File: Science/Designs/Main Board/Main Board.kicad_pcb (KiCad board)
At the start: 2 copper layers, 127 x 101.6 mm, 93 parts, among them J1 I2C_OUT, J10 AIR_SENS, J11 MOISTURE_SENS, J12 LIMIT3, J13 LIMIT2, J14 LIMIT1, J15 SERVO3, J16 SERVO2, J17 SERVO1, J18 MOTOR1_SIG, J19 MOTOR2_SIG, J2 ANE_SENS, J20 MOTOR3_SIG, J4 ENCODER2, J5 ENCODER1, J7 ATMO_SENS, P1 LS7366R, P2 LS7366R, P3 RPI_HEADER, P4 PWR_IN, P5 UV_SENS, P6 DIST_SENS, P7 I2C_TEST, P8 THERMO_SENS, P9 SPI_TEST, U1 SN74HC14N, U2 TLV2544ID, U3 PCA9685, U4 PCA9685, U5 ACPL-064L-500E, U6 ACPL-064L-500E, U7 LM317T, Y1 20MHz, Y2 20MHz

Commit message: Layout nearing completion.
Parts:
- C1, C16, C17, C2, C3, C8, R1, R13, R2, R3, R37, R38, R39, R4, R5, R6, U1, U5, U6: moved to B.Cu
- moved R6 80.1 mm to (131.4, 59.1), turned to 270 degrees
- moved C3 78.1 mm to (127.6, 59.1), turned to 90 degrees
- moved R5 75.4 mm to (122.6, 59.1), turned to 270 degrees
- moved C8 75.1 mm to (116.2, 73.0), turned to 180 degrees
- moved C2 74.1 mm to (118.7, 59.1), turned to 90 degrees
- moved U1 73.7 mm to (116.2, 67.3)
- moved R4 72.3 mm to (113.7, 59.1), turned to 270 degrees
- moved C1 71.9 mm to (109.9, 59.1), turned to 90 degrees
- moved C17 53.3 mm to (111.8, 122.6), turned to 180 degrees
- moved C16 51.9 mm to (111.8, 132.7), turned to 180 degrees
- moved R1 49.5 mm to (140.3, 106.7), turned to 180 degrees
- moved R3 47.5 mm to (132.7, 106.7), turned to 0 degrees
- moved R2 46.7 mm to (140.3, 92.7), turned to 180 degrees
- moved U6 45.7 mm to (111.8, 117.5), turned to 0 degrees
- moved R13 44.6 mm to (132.7, 92.7), turned to 0 degrees
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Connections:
- P3 pad 16: /PI_SS_0 -> /PI_SS_3
- P3 pad 18: /PI_SS_1 -> /PI_SS_2
- P3 pad 29: /PI_SS_2 -> /PI_SS_1
- P3 pad 31: /PI_SS_3 -> /PI_SS_0
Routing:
- net +3V3: track 176.4 -> 320.4 mm
- net /ENC1_A: track 0.00 -> 111.3 mm, vias 0 -> 1
- net /PI_SCL: track 66.4 -> 172.0 mm, vias 2 -> 3
- net /PI_SDA: track 70.8 -> 172.0 mm, vias 2 -> 3
- net /MOTOR3_OUT: track 0.00 -> 100.2 mm
- net /ENC1_B: track 0.00 -> 90.5 mm, vias 0 -> 1
- net /MOTOR2_OUT: track 0.00 -> 89.2 mm
- net /MOTOR1_OUT: track 0.00 -> 79.0 mm
- net /PI_SS_0: track 0.00 -> 74.2 mm, vias 0 -> 2
- net /LIM3_OUT: track 0.00 -> 70.5 mm, vias 0 -> 1
- net /LIM2_OUT: track 0.00 -> 65.1 mm, vias 0 -> 1
- net /LIM1_OUT: track 0.00 -> 61.6 mm, vias 0 -> 1
- net /PI_SS_1: track 0.00 -> 53.0 mm
- net /PI_SCK: track 98.3 -> 142.8 mm
- net /PI_MISO: track 100.8 -> 142.7 mm
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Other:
- board text added: "AIRQ"
- board text added: "ANEM"
- board text added: "ATMO"
- board text added: "DIST"
- board text added: "ENC1"
- board text added: "ENC2"
- board text added: "I2C"
- board text added: "LIM1"
- board text added: "LIM2"
- board text added: "LIM3"
- board text added: "MOIST"
- board text added: "MOT1"
- board text added: "MOT2"
- board text added: "MOT3"
- board text added: "SERV1"
- board text added: "SERV2"
- board text added: "SERV3"
- board text added: "THERM"
- board text added: "UV"
- board text removed: "1"
- board text removed: "2"
- board text removed: "3"
- board text removed: "ENCODER"
- board text removed: "LIMIT SW"

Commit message: Continued work on main board layout. Nearing completion!
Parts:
- C18, C19, R40, R41: moved to B.Cu
- moved U7 51.2 mm to (124.5, 111.1), turned to 90 degrees
- moved C18 15.3 mm to (169.9, 87.9), turned to 90 degrees
- moved R40 8.62 mm to (172.4, 101.9), turned to 0 degrees
- moved HS1 7.16 mm to (121.0, 108.6)
- moved C19 6.74 mm to (177.5, 94.3), turned to 270 degrees
- moved R41 5.22 mm to (172.4, 98.7), turned to 0 degrees
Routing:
- net +5V: track 46.2 -> 213.3 mm
- net /PI_MISO: track 142.7 -> 257.7 mm, vias 0 -> 2
- net /PI_SCK: track 142.8 -> 239.5 mm, vias 0 -> 1
- net /PI_MOSI: track 66.6 -> 155.1 mm, vias 1 -> 3
- net +12V: track 0.00 -> 79.1 mm
- net +3V3: track 320.4 -> 395.9 mm, vias 0 -> 4
- net /PI_SDA: track 172.0 -> 183.1 mm
- net /PI_SCL: track 172.0 -> 182.5 mm
- net /LIM2_RAW: track 26.7 -> 22.5 mm
- net /ENC1_A: track 111.3 -> 110.6 mm
- net /LED_6R: track 19.7 -> 19.0 mm
- net /LED_3R: track 26.9 -> 27.6 mm
- net /RGB_5R: track 27.2 -> 26.4 mm

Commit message: Continuing layout work
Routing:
- net /ENC2_A: track 0.00 -> 104.0 mm, vias 0 -> 1
- net /ENC2_B: track 0.00 -> 98.3 mm, vias 0 -> 1
- net +3V3: track 395.9 -> 462.6 mm, vias 4 -> 6
- net +5V: track 213.3 -> 242.6 mm, vias 0 -> 1
- net /ENC1_B: track 90.5 -> 103.9 mm
- net /PI_SDA: track 183.1 -> 189.0 mm, vias 3 -> 5
- net /PI_SCL: track 182.5 -> 188.0 mm, vias 3 -> 5
- net /ENC1_A: track 110.6 -> 107.0 mm
- net /PI_MISO: track 257.7 -> 254.9 mm
- net /PI_MOSI: track 155.1 -> 152.6 mm
- net /PI_SCK: track 239.5 -> 237.0 mm

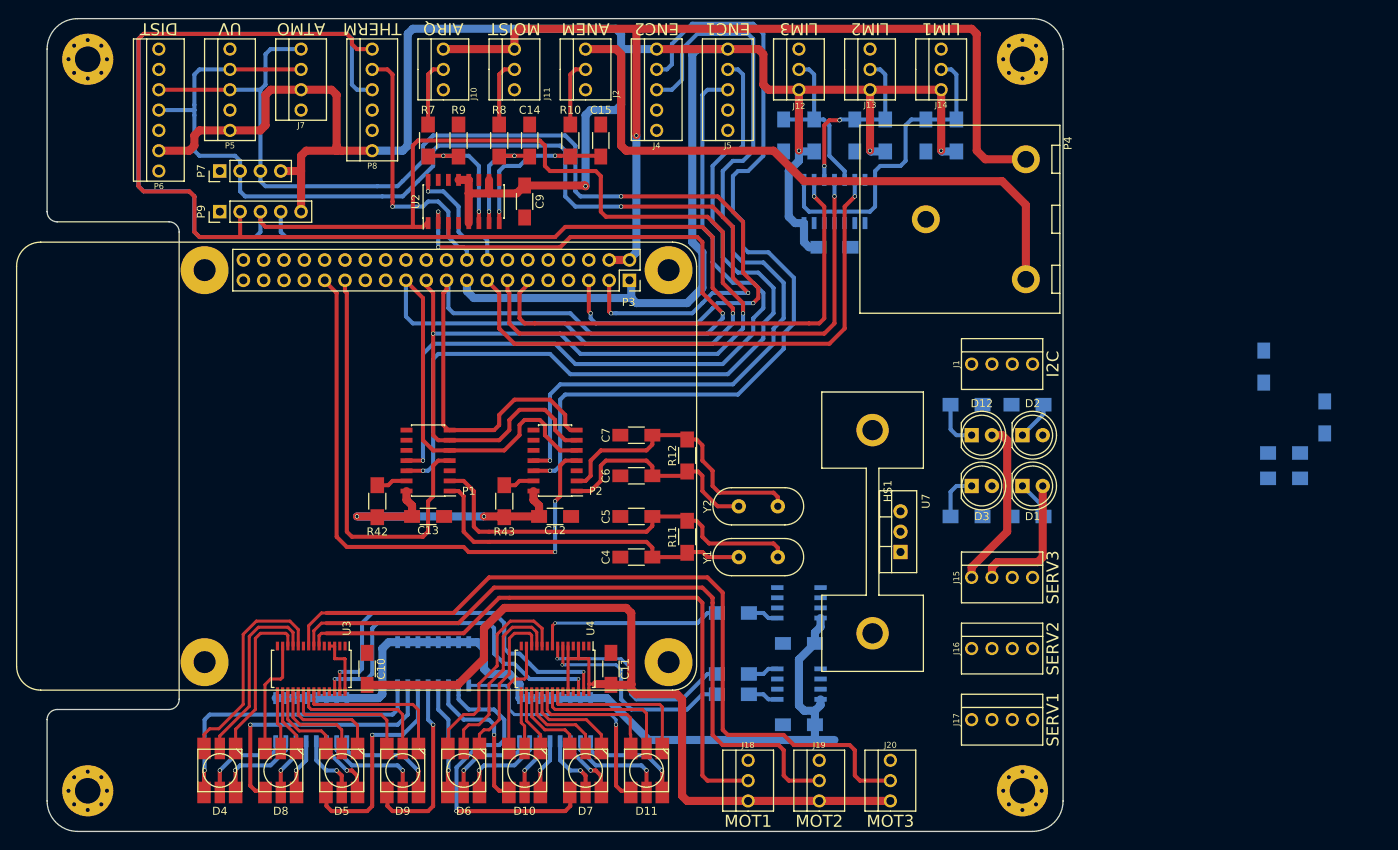
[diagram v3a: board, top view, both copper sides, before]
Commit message: Very close to finished main board
Just needs ground plane work now!
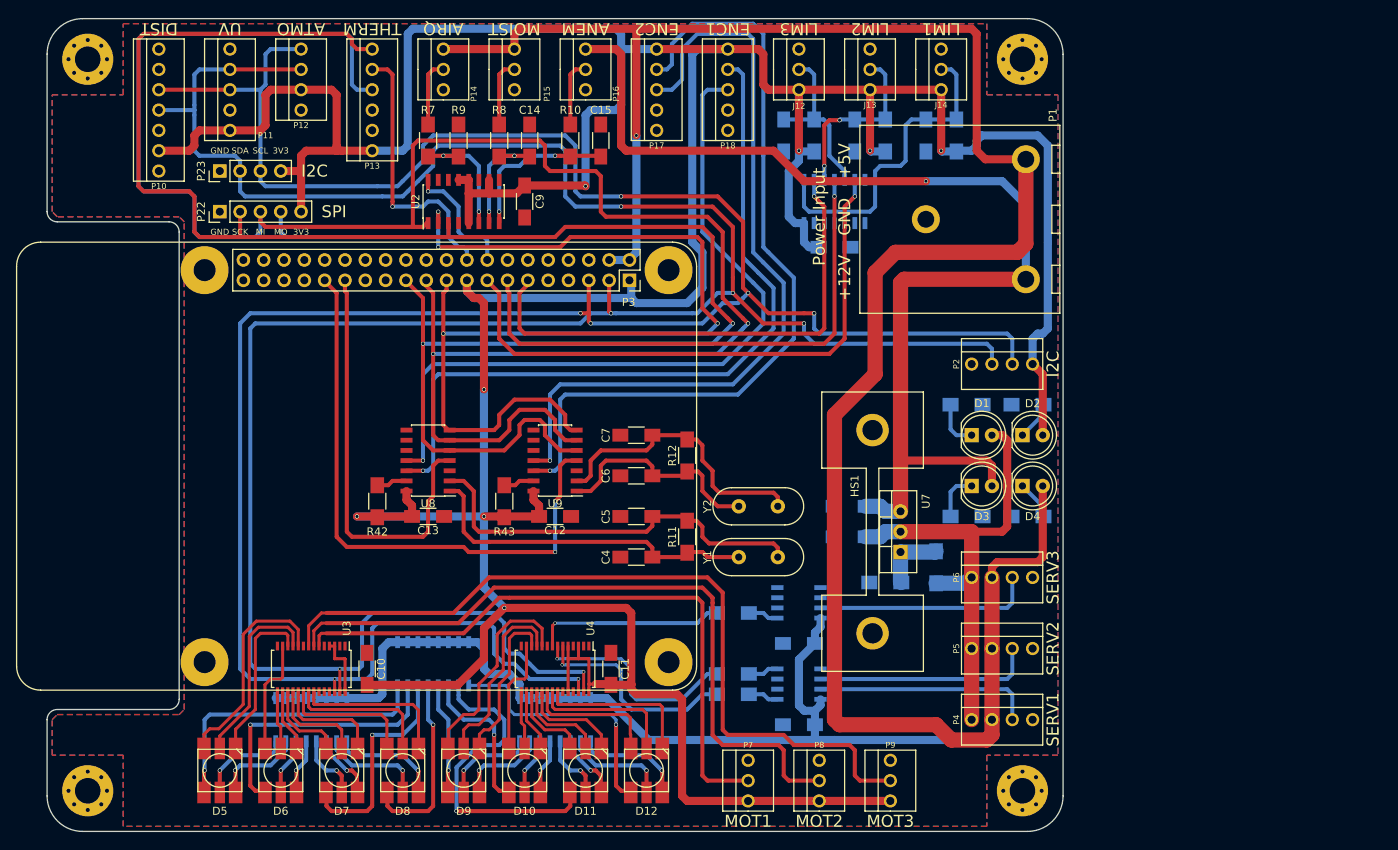
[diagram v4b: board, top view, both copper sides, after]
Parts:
- removed the P1 at (65.4, 99.7)
- removed the P2 at (81.3, 99.7)
- added U8: LS7366R, Housings_SOIC:SOIC-14_3.9x8.7mm_Pitch1.27mm, F.Cu at (65.4, 99.7)
- added U9: LS7366R, Housings_SOIC:SOIC-14_3.9x8.7mm_Pitch1.27mm, F.Cu at (81.3, 99.7)
- moved C19 61.2 mm to (118.1, 109.2), turned to 180 degrees
- moved C18 54.6 mm to (118.1, 105.4), turned to 180 degrees
- moved R40 51.5 mm to (122.6, 114.9)
- moved R41 45.8 mm to (128.9, 113.0), turned to 90 degrees
- renumbered D12 to D1, D7 to D11, D11 to D12, D1 to D4, D4 to D5, D8 to D6, D5 to D7, D9 to D8, D6 to D9, P4 to P1, P6 to P10, P5 to P11, J7 to P12, P8 to P13, J10 to P14, J11 to P15, J2 to P16, J4 to P17, J5 to P18, J1 to P2, P9 to P22, P7 to P23, J17 to P4, J16 to P5, J15 to P6, J18 to P7, J19 to P8, J20 to P9
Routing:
- net +5V: track 242.6 -> 394.0 mm
- net /PI_SCL: track 188.0 -> 325.5 mm, vias 5 -> 7
- net /PI_SDA: track 189.0 -> 323.4 mm, vias 5 -> 6
- net +3V3: track 462.6 -> 556.9 mm, vias 6 -> 8
- net +12V: track 79.1 -> 142.4 mm, vias 0 -> 1
- net /7.2V: track 21.2 -> 59.4 mm
- net /SERVO1_PWM: track 0.00 -> 27.4 mm
- net /SERVO3_PWM: track 0.00 -> 27.4 mm
- net /SERVO2_PWM: track 0.00 -> 27.4 mm
- net /ENC2_A: track 104.0 -> 95.1 mm
- net Net-(R40-Pad2): track 0.00 -> 8.33 mm
- net /PI_SCK: track 237.0 -> 228.9 mm, vias 1 -> 2
- net /ENC1_B: track 103.9 -> 98.5 mm
- net /ENC1_A: track 107.0 -> 101.6 mm
- net /ENC2_B: track 98.3 -> 93.2 mm
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- added copper zone on B.Cu, net GNDD
- added copper zone on F.Cu, net GNDD
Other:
- outline, holes or cut-outs redrawn
- board text added: "+12V"
- board text added: "+5V"
- board text added: "3V3"
- board text added: "GND"
- board text added: "MI"
- board text added: "MO"
- board text added: "Power Input"
- board text added: "SCK"
- board text added: "SCL"
- board text added: "SDA"
- board text added: "SPI"

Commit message: Ground planes almost done
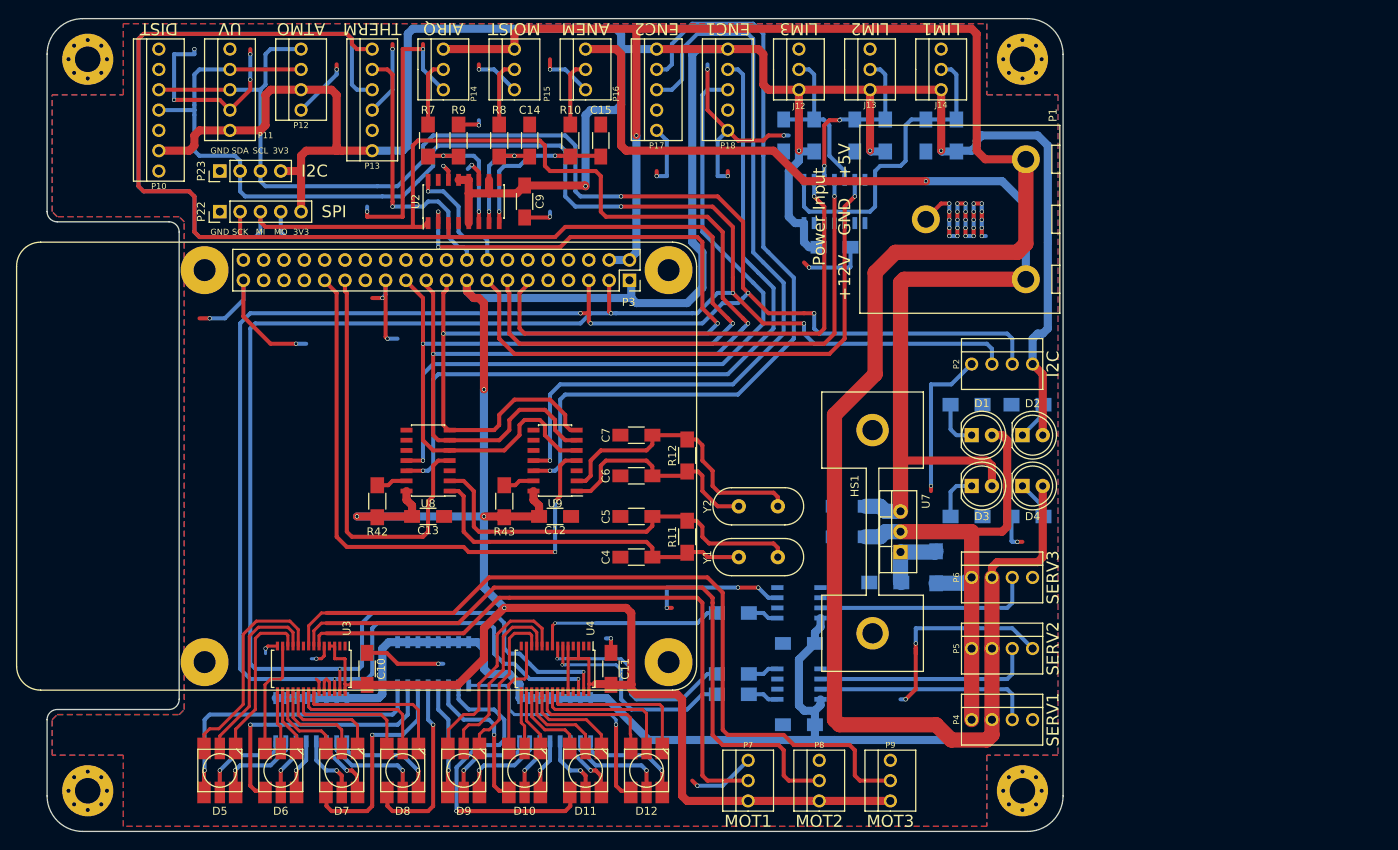
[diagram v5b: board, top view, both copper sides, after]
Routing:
- net GNDD: track 0.00 -> 310.4 mm, vias 0 -> 60
- net +3V3: track 556.9 -> 559.7 mm

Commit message: Main Board finished?
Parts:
- moved R1 6.99 mm to (140.3, 99.7)
- moved R3 6.99 mm to (132.7, 99.7)
- moved R41 3.81 mm to (128.9, 116.8)
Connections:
- P3 pad 20: GNDD -> Net-(P3-Pad20)
- P3 pad 30: GNDD -> Net-(P3-Pad30)
- P3 pad 34: GNDD -> Net-(P3-Pad34)
- P3 pad 9: GNDD -> Net-(P3-Pad9)
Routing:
- net GNDD: track 310.4 -> 346.3 mm, vias 60 -> 66
- net /MOTOR3_OUT: track 100.2 -> 102.8 mm
- net /MOTOR2_OUT: track 89.2 -> 91.8 mm
- net /MOTOR1_OUT: track 79.0 -> 81.6 mm
- net /PI_SS_2: track 34.5 -> 36.3 mm
- net Net-(D3-Pad1): track 6.02 -> 4.27 mm
- net /SERVO3_PWM: track 27.4 -> 29.1 mm
- net /RGB_5R: track 26.4 -> 28.1 mm
- net /7.2V: track 59.4 -> 61.1 mm
- net /RGB_5G: track 23.5 -> 25.0 mm
- net /RGB_5B: track 20.2 -> 21.7 mm
- net Net-(D4-Pad1): track 4.90 -> 4.27 mm
- net /PI_SDA: vias 6 -> 7
- net /PI_SCL: vias 7 -> 8
- net +3V3: vias 8 -> 9

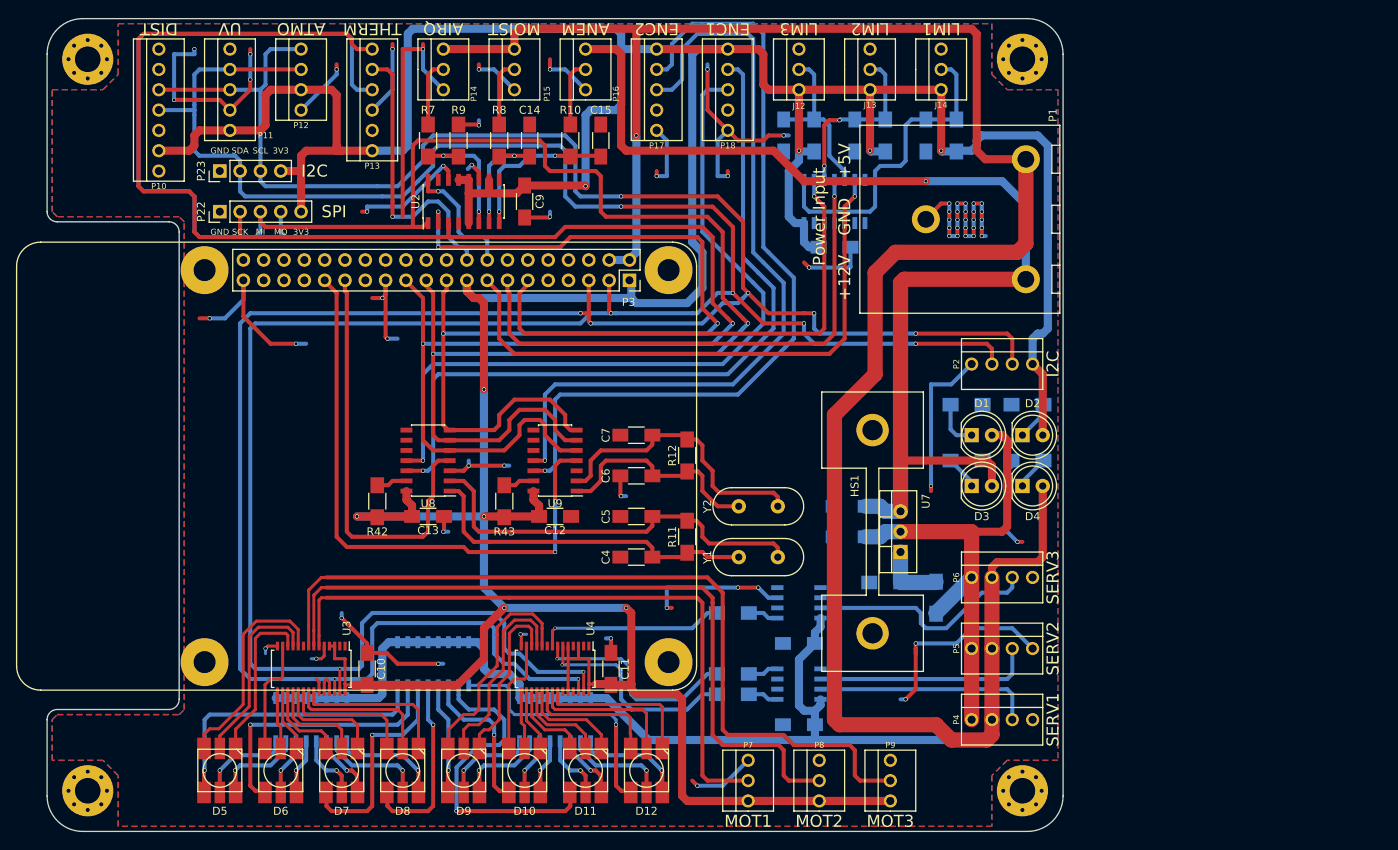
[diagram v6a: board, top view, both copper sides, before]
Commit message: Fixing issues, adding logos
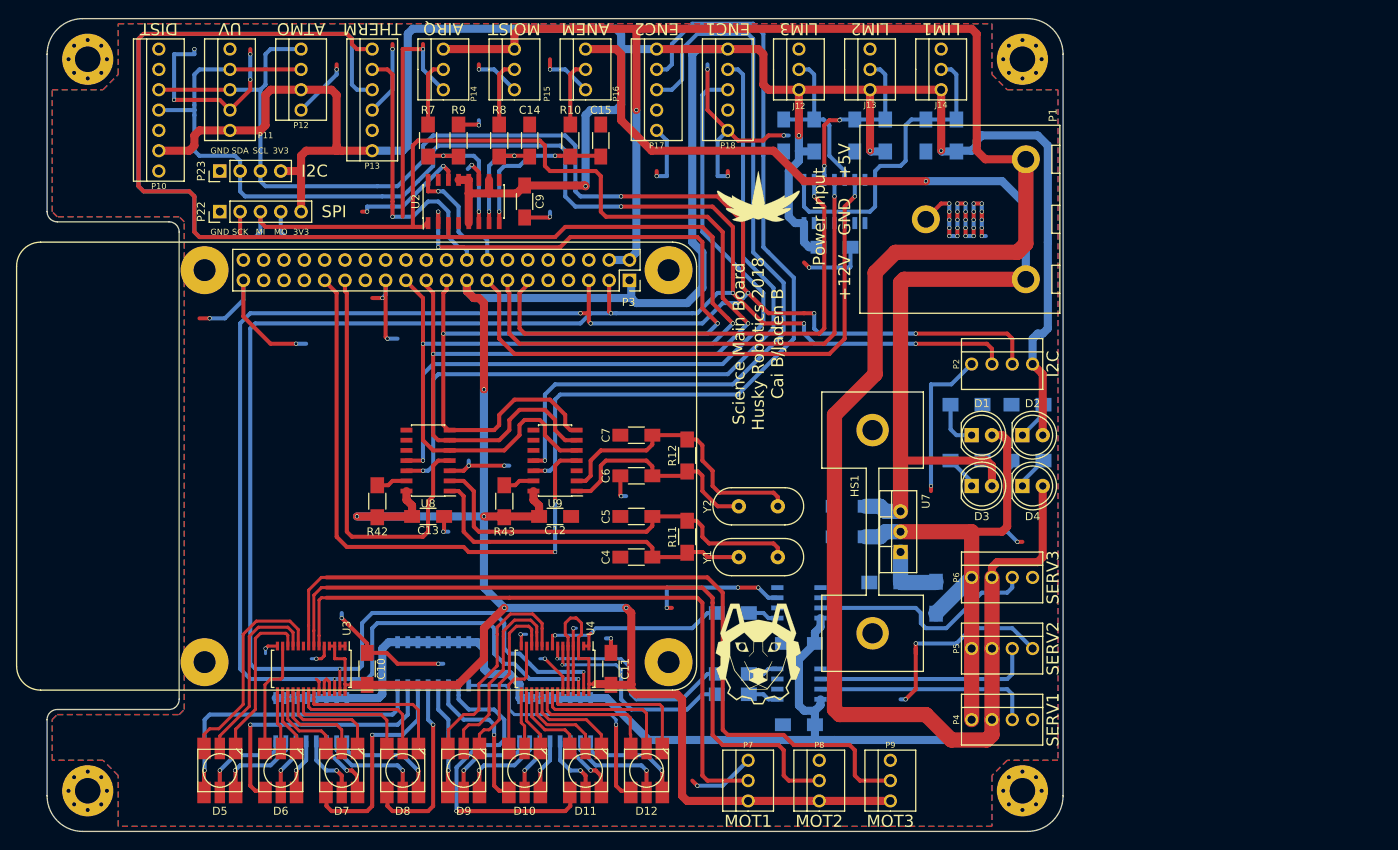
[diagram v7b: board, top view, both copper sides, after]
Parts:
- added G***: LOGO, ScienceFootprints:Scarlet-0.50in, F.Cu at (106.7, 66.7)
- added G***: LOGO, ScienceFootprints:Husky-0.50in, F.Cu at (106.7, 123.8)
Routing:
- net GNDD: track 346.3 -> 363.3 mm, vias 66 -> 68
- net +3V3: track 559.7 -> 567.1 mm
- net +12V: track 142.4 -> 140.5 mm
- net +5V: track 394.0 -> 393.3 mm
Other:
- net class Default: clearance 0.254 -> 0.1524
- rule trace_clearance: 0.254 -> 0.1524
- board text added: "Science Main Board Husky Robotics 2018 Cai B/Jaden B"

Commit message: Last-minute changes and production output for main board
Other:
- board text added: "7.2V / 3.3V 12V / 5V"
- board text added: "Don't forget. Always, somewhere, someone is fighting for you. As long as you remember her, you are not alone."
